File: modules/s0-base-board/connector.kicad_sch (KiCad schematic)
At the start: 2 parts

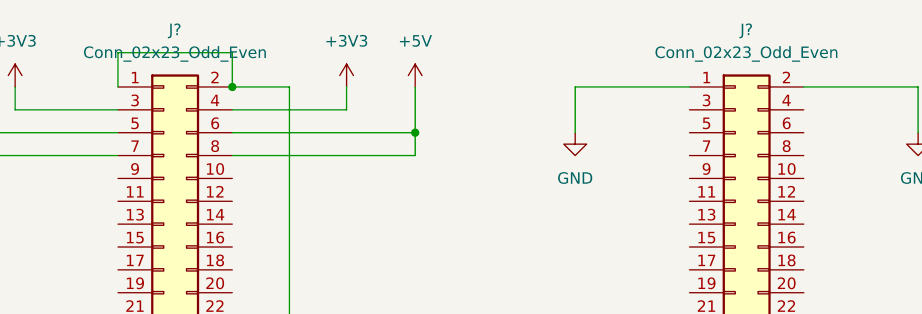
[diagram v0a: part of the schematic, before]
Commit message: feat(pcb): update schematic with PCB
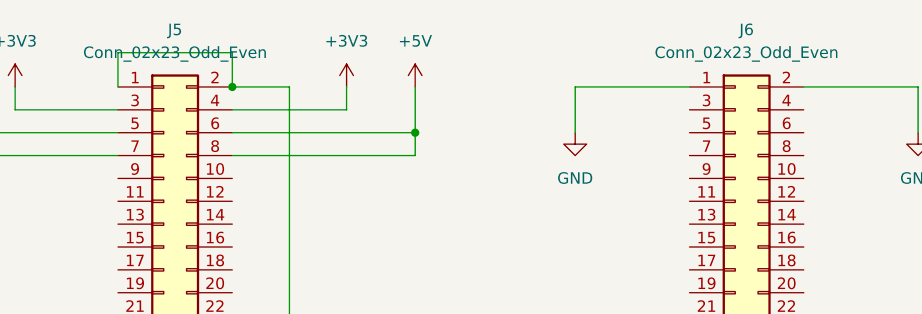
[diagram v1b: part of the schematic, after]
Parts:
- J5, J6: renamed from J?; footprint (none) -> Connector_PinHeader_2.54mm:PinHeader_2x23_P2.54mm_Vertical
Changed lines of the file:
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@@
 		(dnp no)
 		(fields_autoplaced yes)
-		(property "Reference" "J?"
+		(property "Reference" "J6"
 			(at 148.59 45.72 0)
 			(effects
@@
 			)
 		)
-		(property "Footprint" ""
+		(property "Footprint" "Connector_PinHeader_2.54mm:PinHeader_2x23_P2.54mm_Vertical"
 			(at 147.32 80.01 0)
 			(effects
@@
 			(project "s0-base-board"
 				(path "/30a07aa9-a4c6-42ad-8aa6-f5766a70e64f/5fd7a6a7-9e92-4e1d-8156-8c064725d4fa"
-					(reference "J?")
+					(reference "J6")
 					(unit 1)
 				)
@@
 		(dnp no)
 		(fields_autoplaced yes)
-		(property "Reference" "J?"
+		(property "Reference" "J5"
 			(at 85.09 45.72 0)
 			(effects
@@
 			)
 		)
-		(property "Footprint" ""
+		(property "Footprint" "Connector_PinHeader_2.54mm:PinHeader_2x23_P2.54mm_Vertical"
 			(at 83.82 80.01 0)
 			(effects
@@
 			(project ""
 				(path "/30a07aa9-a4c6-42ad-8aa6-f5766a70e64f/5fd7a6a7-9e92-4e1d-8156-8c064725d4fa"
-					(reference "J?")
+					(reference "J5")
 					(unit 1)
 				)

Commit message: Production build
Signed-off-by: Rodney Osodo <socials@rodneyosodo.com>
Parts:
- added U6: BEAGLEBONEBLACK, modules:BB_Cape, symbol BEAGLEBONEBLACK:BEAGLEBONEBLACK
- J5, J6: footprint Connector_PinHeader_2.54mm:PinHeader_2x23_P2.54mm_Vertical -> Connector_PinSocket_2.54mm:PinSocket_2x23_P2.54mm_Vertical
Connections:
- new net: U6.J1_1 (DGND), U6.P8_1 (DGND), U6.P8_2 (DGND), U6.P9_1 (DGND), U6.P9_2 (DGND), U6.P9_43 (DGND), U6.P9_44 (DGND), U6.P9_45 (DGND), U6.P9_46 (DGND)
- new net: U6.J1_2 (NC), U6.J1_3 (NC), U6.J1_6 (NC)
- new net: U6.P1 (SHIELD), U6.P2 (SHIELD), U6.P3 (SHIELD), U6.P4 (SHIELD)
- new net: U6.P9_3 (VDD_3V3B), U6.P9_4 (VDD_3V3B)
- new net: U6.P9_5 (VDD_5V), U6.P9_6 (VDD_5V)
- new net: U6.P9_7 (SYS_5V), U6.P9_8 (SYS_5V)
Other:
- moved on the sheet: J5, J6

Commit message: Documentation added onto Schematic
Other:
- note added: "BeagleBone Cape Board"
- note added: "Female Pin Headers connected to the BeagleBone Cape"
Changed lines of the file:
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@@
 		(company "Abstract Machines")
 		(comment 1 "Deigned By: Rodney Osodo")
-		(comment 2 "Approved By:")
+		(comment 2 "Approved By: Jones Kisaka")
 	)
 	(junction
@@
 		)
 	)
+	(text "BeagleBone Cape Board"
+		(exclude_from_sim no)
+		(at 133.858 31.496 0)
+		(effects
+			(font
+				(size 2.5 2.5)
+			)
+		)
+	)
+	(text "Female Pin Headers connected to the BeagleBone Cape"
+		(exclude_from_sim no)
+		(at 203.962 43.688 0)
+		(effects
+			(font
+				(size 1.27 1.27)
+			)
+		)
+	)

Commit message: feat(base): add schematic notes and PCB notes
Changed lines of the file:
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@@
 	(text "BeagleBone Cape Board"
 		(exclude_from_sim no)
-		(at 133.858 31.496 0)
+		(at 94.234 22.606 0)
 		(effects
 			(font
-				(size 2.5 2.5)
+				(size 5 5)
+				(thickness 1)
+				(bold yes)
 			)
+			(justify left bottom)
 		)
 	)

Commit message: JLCPCB Modified parts
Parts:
- J5, J6: JLCPCB (none) -> C27985238
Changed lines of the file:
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@@
+			)
+		)
+		(property "JLCPCB" "C27985238"
+			(at 237.49 88.9 0)
+			(effects
+				(font
+					(size 1.27 1.27)
+				)
+				(hide yes)
 			)
 		)
@@
 			(at 173.99 88.9 0)
 			(effects
+				(font
+					(size 1.27 1.27)
+				)
+				(hide yes)
+			)
+		)
+		(property "JLCPCB" "C27985238"
+			(at 173.99 88.9 0)
+			(effects

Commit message: Updated PCB from reviews
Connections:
- net +3V3: now also J6.3 (Pin_3), J6.4 (Pin_4); no longer J5.3 (Pin_3), J5.4 (Pin_4)
- net +5V: now also J6.5 (Pin_5), J6.6 (Pin_6), J6.7 (Pin_7), J6.8 (Pin_8); no longer J5.5 (Pin_5), J5.6 (Pin_6), J5.7 (Pin_7), J5.8 (Pin_8)

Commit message: Reviewed Changes
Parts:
- added TP1, TP2, TP3: TestPoint, TestPoint:TestPoint_Pad_D1.0mm, symbol Connector:TestPoint
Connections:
- net +3V3: now also TP1.1
- net +5V: now also TP2.1
- net GND: now also TP3.1
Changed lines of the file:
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@@
+	)
+	(junction
+		(at 255.27 57.15)
+		(diameter 0)
+		(color 0 0 0 0)
+	)
+	(junction
+		(at 267.97 67.31)
+		(diameter 0)
+		(color 0 0 0 0)
 	)
 	(junction
@@
 	)
 	(junction
+		(at 257.81 71.12)
+		(diameter 0)
+		(color 0 0 0 0)
+	)
+	(junction
 		(at 181.61 121.92)
 		(diameter 0)
@@
 	(wire
 		(pts
-			(xy 255.27 63.5) (xy 255.27 54.61)
+			(xy 255.27 63.5) (xy 255.27 57.15)
 		)
 		(stroke
@@
 	(wire
 		(pts
+			(xy 255.27 57.15) (xy 255.27 54.61)
+		)
+		(stroke
+			(width 0)
+			(type default)
+		)
+	)
+	(wire
+		(pts
 			(xy 168.91 116.84) (xy 168.91 121.92)
 		)
@@
 	(wire
 		(pts
+			(xy 257.81 71.12) (xy 257.81 60.96)
+		)
+		(stroke
+			(width 0)
+			(type default)
+		)
+	)
+	(wire
+		(pts
 			(xy 245.11 67.31) (xy 245.11 68.58)
 		)
@@
 	(wire
 		(pts
-			(xy 257.81 73.66) (xy 257.81 60.96)
+			(xy 257.81 73.66) (xy 257.81 71.12)
 		)
 		(stroke
@@
 				(path "/30a07aa9-a4c6-42ad-8aa6-f5766a70e64f/5fd7a6a7-9e92-4e1d-8156-8c064725d4fa"
 					(reference "#PWR064")
+					(unit 1)
+				)
+			)
+		)
+	)
+	(symbol
+		(lib_id "Connector:TestPoint")
+		(at 257.81 71.12 270)
+		(unit 1)
+		(exclude_from_sim no)
+		(in_bom yes)
+		(on_board yes)
+		(dnp no)
+		(fields_autoplaced yes)
+		(property "Reference" "TP3"
+			(at 262.89 69.8499 90)
+			(effects
+				(font
+					(size 1.27 1.27)
+				)
+				(justify left)
+			)
+		)
+		(property "Value" "TestPoint"
+			(at 262.89 72.3899 90)
+			(effects
+				(font
+					(size 1.27 1.27)
+				)
+				(justify left)
+			)
+		)
+		(property "Footprint" "TestPoint:TestPoint_Pad_D1.0mm"
+			(at 257.81 76.2 0)
+			(effects
+				(font
+					(size 1.27 1.27)
+				)
+				(hide yes)
+			)
+		)
+		(property "Datasheet" "~"
+			(at 257.81 76.2 0)
+			(effects
+				(font
+					(size 1.27 1.27)
+				)
+				(hide yes)
+			)
+		)
+		(property "Description" "test point"
+			(at 257.81 71.12 0)
+			(effects
+				(font
+					(size 1.27 1.27)
+				)
+				(hide yes)
+			)
+		)
+		(pin "1"
+		)
+		(instances
+			(project "s0-base-board"
+				(path "/30a07aa9-a4c6-42ad-8aa6-f5766a70e64f/5fd7a6a7-9e92-4e1d-8156-8c064725d4fa"
+					(reference "TP3")
 					(unit 1)
 				)
@@
 					(unit 1)
 				)
+			)
+		)
+	)
+	(symbol
+		(lib_id "Connector:TestPoint")
+		(at 255.27 57.15 270)
+		(unit 1)
+		(exclude_from_sim no)
+		(in_bom yes)
+		(on_board yes)
+		(dnp no)
+		(fields_autoplaced yes)
+		(property "Reference" "TP1"
+			(at 260.35 55.8799 90)
+			(effects
+				(font
+					(size 1.27 1.27)
+				)
+				(justify left)
+			)
+		)
+		(property "Value" "TestPoint"
+			(at 260.35 58.4199 90)
+			(effects
+				(font
+					(size 1.27 1.27)
+				)
+				(justify left)
+			)
+		)
+		(property "Footprint" "TestPoint:TestPoint_Pad_D1.0mm"
+			(at 255.27 62.23 0)
+			(effects
+				(font
+					(size 1.27 1.27)
+				)
+				(hide yes)
+			)
+		)
+		(property "Datasheet" "~"
+			(at 255.27 62.23 0)
+			(effects
+				(font
+					(size 1.27 1.27)
+				)
+				(hide yes)
+			)
+		)
+		(property "Description" "test point"
+			(at 255.27 57.15 0)
+			(effects
+				(font
+					(size 1.27 1.27)
+				)
+				(hide yes)
+			)
+		)
+		(pin "1"
+		)
+		(instances
+			(project ""
+				(path "/30a07aa9-a4c6-42ad-8aa6-f5766a70e64f/5fd7a6a7-9e92-4e1d-8156-8c064725d4fa"
+					(reference "TP1")
+					(unit 1)
+				)
+			)
+		)
+	)
+	(symbol
+		(lib_id "Connector:TestPoint")
+		(at 267.97 67.31 270)
+		(unit 1)
+		(exclude_from_sim no)
+		(in_bom yes)
+		(on_board yes)
+		(dnp no)
+		(fields_autoplaced yes)
+		(property "Reference" "TP2"
+			(at 273.05 66.0399 90)
+			(effects
+				(font
+					(size 1.27 1.27)
+				)
+				(justify left)
+			)
+		)
+		(property "Value" "TestPoint"
+			(at 273.05 68.5799 90)
+			(effects
+				(font
+					(size 1.27 1.27)
+				)
+				(justify left)
+			)
+		)
+		(property "Footprint" "TestPoint:TestPoint_Pad_D1.0mm"
+			(at 267.97 72.39 0)
+			(effects
+				(font
+					(size 1.27 1.27)
+				)
+				(hide yes)
+			)
+		)
+		(property "Datasheet" "~"
+			(at 267.97 72.39 0)
+			(effects
+				(font
+					(size 1.27 1.27)
+				)
+				(hide yes)
+			)
+		)
+		(property "Description" "test point"
+			(at 267.97 67.31 0)
+			(effects
+				(font
+					(size 1.27 1.27)
+				)
+				(hide yes)
+			)
+		)
+		(pin "1"
+		)
+		(instances
+			(project "s0-base-board"
+				(path "/30a07aa9-a4c6-42ad-8aa6-f5766a70e64f/5fd7a6a7-9e92-4e1d-8156-8c064725d4fa"
+					(reference "TP2")
+					(unit 1)
+				)
